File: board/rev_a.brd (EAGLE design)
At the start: 56 x 25 mm, 12 parts, among them IC1 STM32-M-48, IC2 LM2936DT-5.0, IC3 MCP6004, Q1 35A/25V/8.5mΩ, U1 3.3V/150mA

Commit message: [board] Updated PCB and IOC files
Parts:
- removed IC2: LM2936DT-5.0, national-semiconductor:TO252
- removed U1: 3.3V/150mA, SparkFun-IC-Power:SOT23-5
- added C1: 47pF, resistor:C0603
- added D2, D3: BAT54S, diode:SOT23
- added IC4: 25LC040ST, microchip:TSSOP8
- added LDO1: LM2936DT-5.0, national-semiconductor:TO252
- added LDO2: 3.3V/150mA, SparkFun-IC-Power:SOT23-5
- added MCU: STM32-M-48, pel_stm32:LQFP48
- added OP1: MCP6004, linear:TSSOP14
- added Q2: 600mA/40V, SparkFun-DiscreteSemi:SOT23-3
- added R3: 22K, resistor:R0603
- added R4, R5: 1K, resistor:R0603
- added RN1, RN2: 1K, resistor-dil:0603-ARC
- IC1: value STM32-M-48 -> TJA1027; device pel_stm32:LQFP48 -> misc:SO08
- IC3: value MCP6004 -> MCP2551; device linear:TSSOP14 -> SparkFun-IC-Comms:SO08
- moved R2 54.3 mm to (16.0, 21.0), turned to 180 degrees
- moved IC1 34.2 mm to (5.00, 3.00), turned to 270 degrees
- moved C2 14.0 mm to (37.0, 3.75)
- moved C3 13.1 mm to (20.5, 12.5)
- moved IC3 12.0 mm to (20.5, 3.00), turned to 90 degrees
- moved R1 10.3 mm to (12.5, 21.0)
- moved Q1 5.70 mm to (5.62, 21.0)
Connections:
- net N$4 renamed HEATER_CTRL
- new net CAN_CSN: IC3.8, R3.1
- new net CAN_RX: IC3.4, MCU.45
- new net CAN_TX: IC3.1, MCU.46
- new net KLINE: IC1.6, R5.2
- new net KLINE_PULLUP: R4.1
- new net LED_B: RN1.5
- new net LED_G: RN1.7
- new net LED_R: RN1.6
- new net N$1: Q2.3, R5.1
- new net N$10: OP1.7
- new net N$11: OP1.1
- new net N$3: D1.4, RN1.4
- new net N$4: C1.1, LDO2.4
- new net N$5: D1.6, RN1.2
- new net N$6: D1.5, RN1.3
- new net N$7: Q2.1, R4.2
- new net OUT1: D2.3, IC3.7, OP1.8, RN2.7, RN2.8
- new net OUT1_C: J1.3, RN2.1, RN2.2
- new net OUT2: D3.3, IC3.6, OP1.14, RN2.5, RN2.6
- new net OUT2_C: J1.2, RN2.3, RN2.4
- new net SPI2_CLK: IC4.6, MCU.26
- new net SPI2_CS: IC4.1
- new net SPI2_MISO: IC4.2, MCU.27
- new net SPI2_MOSI: IC4.5, MCU.28
- new net USART_CS: IC1.2
- new net USART_RX: IC1.1
- new net USART_TX: IC1.4
- net 12V: now also IC1.7, LDO1.1, Q2.2; no longer IC2.1
- net 5V: now also D1.2, D1.3, D2.2, D3.2, IC3.3, LDO1.3, LDO2.1, LDO2.3, OP1.4; no longer IC2.3, IC3.4, U1.1, U1.3
- net GND: now also C1.2, D2.1, D3.1, IC1.5, IC3.2, IC4.3, IC4.4, IC4.7, LDO1.2, LDO2.2, MCU.23, MCU.35, MCU.47, OP1.11, R3.2; no longer IC1.23, IC1.35, IC1.47, IC2.2, IC3.11, U1.2
- net VBAT: now also MCU.1; no longer IC1.1
- net VCC: now also IC1.3, IC4.8, LDO2.5, MCU.24, MCU.36, MCU.48, MCU.9; no longer IC1.24, IC1.36, IC1.48, IC1.9, U1.5
- net VSSA: now also MCU.8; no longer IC1.8

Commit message: [board] Cleaning up
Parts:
- removed IC1: TJA1027, misc:SO08
- removed IC4: 25LC040ST, microchip:TSSOP8
- removed Q2: 600mA/40V, SparkFun-DiscreteSemi:SOT23-3
- removed R1, R4, R5: 1K, resistor:R0603
- removed R2: 10K, resistor:R0603
- added RN3: 1K, resistor-dil:0603-ARC
- added S1: (no value), SparkFun-Switches:TACTILE_SWITCH_SMD_5.2MM
- moved C1 127.7 mm to (40.5, 22.0), turned to 90 degrees
- moved R3 56.1 mm to (11.0, 1.00)
- moved D1 19.5 mm to (31.0, 3.00)
- moved RN1 19.5 mm to (36.5, 3.25)
- moved C2 19.1 mm to (42.5, 22.0), turned to 90 degrees
- moved LDO2 18.6 mm to (37.6, 21.9), turned to 180 degrees
- moved IC3 16.5 mm to (4.00, 3.00)
- moved OP1 8.25 mm to (27.0, 20.8), turned to 90 degrees
- moved C3 2.50 mm to (20.5, 10.0), turned to 90 degrees
- moved MCU 0.15 mm to (37.6, 12.7), turned to 90 degrees
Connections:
- net CAN_CSN renamed N$8
- removed net KLINE: IC1.6, R5.2
- removed net KLINE_PULLUP: R4.1
- removed net LED_B: RN1.5
- removed net LED_G: RN1.7
- removed net LED_R: RN1.6
- removed net OUT1_C: J1.3, RN2.1, RN2.2
- removed net OUT2_C: J1.2, RN2.3, RN2.4
- removed net SPI2_CLK: IC4.6, MCU.26
- removed net SPI2_CS: IC4.1
- removed net SPI2_MISO: IC4.2, MCU.27
- removed net SPI2_MOSI: IC4.5, MCU.28
- removed net USART_CS: IC1.2
- removed net USART_RX: IC1.1
- removed net USART_TX: IC1.4
- new net AN1: MCU.10
- new net AN2: MCU.16
- new net AN3: MCU.17
- new net BUTTON1: MCU.2, S1.1, S1.2
- new net CAN_RS: MCU.3, R3.2
- new net DAC1: MCU.14
- new net DAC2: MCU.15
- new net NRST: MCU.7
- new net OPA1_IN+: MCU.11
- new net OPA1_IN-: MCU.13
- new net OPA1_OUT: MCU.12
- new net OPA3_IN+: MCU.18
- new net OPA3_IN-: MCU.20
- new net OPA3_OUT: MCU.19
- new net OPA4_IN+: MCU.22
- new net OPA4_IN-: MCU.21
- new net OPA4_OUT: MCU.25
- new net OUT1_PROT: D2.3, MCU.30, OP1.8, RN2.7, RN2.8
- new net OUT2_PROT: D3.3, MCU.31, OP1.14, RN2.5, RN2.6
- new net SWDCLK: MCU.37
- new net SWDIO: MCU.34
- new net TIM2_CH2: MCU.28
- new net TIM4_CH1: MCU.42, RN1.5
- new net TIM4_CH2: MCU.43, RN1.7
- new net TIM4_CH3: MCU.45, RN1.6
- new net TIM4_CH4: MCU.46
- net 12V: no longer IC1.7, Q2.2
- net 5V: now also D1.1
- net CAN_RX: now also MCU.32; no longer MCU.45
- net CAN_TX: now also MCU.33; no longer MCU.46
- net GND: now also RN3.5, S1.3, S1.4; no longer IC1.5, IC4.3, IC4.4, IC4.7, R2.1, R3.2
- net HEATER_CTRL: now also MCU.27, RN3.1, RN3.2; no longer R1.1, R2.2
- net N$1: now also Q1.1, RN3.8; no longer Q2.3, R5.1
- net N$2: now also RN3.3, RN3.7; no longer Q1.1, R1.2
- net N$7: now also RN3.4, RN3.6; no longer Q2.1, R4.2
- net OUT1: now also J1.3, RN2.1, RN2.2; no longer D2.3, OP1.8, RN2.7, RN2.8
- net OUT2: now also J1.2, RN2.3, RN2.4; no longer D3.3, OP1.14, RN2.5, RN2.6
- net VCC: now also MCU.44; no longer IC1.3, IC4.8

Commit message: [board] Testing a few configurations
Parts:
- removed OP1: MCP6004, linear:TSSOP14
- added C4, C5, C6: 100nF, resistor:C0603
- added D4: BAT54S, diode:SOT23
- added J3: (no value), SparkFun-Connectors:1X04_LOCK
- added LDO3: 3.3V/150mA, SparkFun-IC-Power:SOT23-5
- added OPA5: MCP602ST, linear:TSSOP8
- added R1, R4: 20K, resistor:R0603
- added R2, R5: 10K, resistor:R0603
- added R6: 330K, resistor:R0603
- added R7: 22K, resistor:R0603
- added RN4: 1K, resistor-dil:0603-ARC
- D1: value (none) -> BAT54S; device SparkFun-LED:LED-TRICOLOR-5050 -> diode:SOT23
- J1: device SparkFun-Connectors:1X04_LOCK_LONGPADS -> SparkFun-Connectors:1X06_LONGPADS
- LDO1: value LM2936DT-5.0 -> LM2931DT-5.0
- MCU: value STM32-M-48 -> STM32F303CB
- moved Q1 32.8 mm to (38.4, 21.0), turned to 270 degrees
- moved C1 22.9 mm to (18.5, 15.5)
- moved C2 22.2 mm to (23.5, 10.5)
- moved D1 20.7 mm to (10.5, 5.50), turned to 90 degrees
- moved LDO2 20.2 mm to (21.0, 10.5)
- moved S1 20.0 mm to (3.00, 4.00), flipped to the bottom, turned to 90 degrees
- moved RN3 14.5 mm to (29.5, 21.0), turned to 270 degrees
- moved C3 12.3 mm to (25.0, 21.5), turned to 270 degrees
- moved LDO1 9.52 mm to (14.8, 21.2), turned to 270 degrees
- moved R3 8.50 mm to (2.50, 1.00)
- moved D3 8.08 mm to (10.5, 16.0)
- moved D2 8.02 mm to (15.5, 16.0)
- moved RN2 7.00 mm to (6.50, 19.0)
- moved MCU 5.19 mm to (32.8, 11.0), turned to 180 degrees
- moved RN1 2.51 mm to (39.0, 3.00), flipped to the bottom
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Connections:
- removed net N$4: C1.1, LDO2.4
- removed net TIM4_CH1: MCU.42, RN1.5
- removed net TIM4_CH2: MCU.43, RN1.7
- new net N$9: RN1.4, RN1.6
- new net OUT3: IC3.7, J1.3, RN4.1, RN4.2
- new net OUT3_PROT: D1.3, MCU.30, RN4.7, RN4.8
- new net OUT4: IC3.6, J1.2, RN4.3, RN4.4
- new net OUT4_PROT: D4.3, MCU.31, RN4.5, RN4.6
- new net SCL: J3.3, MCU.42, RN1.3
- new net SDA: J3.4, MCU.43, RN1.1
- new net VDDA: C6.1, LDO3.5, MCU.9
- net 12V: now also J1.6; no longer J1.4
- net 5V: now also C5.1, D4.2, J3.2, LDO3.1, LDO3.3, OPA5.8, RN1.5, RN1.7; no longer D1.1, D1.3, OP1.4
- net BUTTON1: now also C4.1
- net DAC1: now also OPA5.3
- net DAC2: now also OPA5.5
- net GND: now also C4.2, C5.2, C6.2, D1.1, D4.1, J3.1, LDO3.2, MCU.44, OPA5.4, R1.1, R4.1; no longer OP1.11
- net IP: now also R7.1
- net N$10: now also R6.1, R7.2; no longer OP1.7
- net N$11: now also C1.1, LDO3.4; no longer OP1.1
- net N$3: now also RN1.2, RN1.8; no longer D1.4, RN1.4
- net N$5: now also OPA5.2, R1.2, R2.2; no longer D1.6, RN1.2
- net N$6: now also R4.2, R5.2; no longer D1.5, RN1.3
- net OPA3_OUT: now also R6.2
- net OUT1: now also J1.5; no longer IC3.7, J1.3
- net OUT1_PROT: now also OPA5.1, R2.1; no longer MCU.30, OP1.8
- net OUT2: now also J1.4; no longer IC3.6, J1.2
- net OUT2_PROT: now also OPA5.7, R5.1; no longer MCU.31, OP1.14
- net TIM4_CH3: no longer RN1.6
- net VCC: no longer MCU.44, MCU.9
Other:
- outline, holes or cut-outs redrawn

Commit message: [board] Working on schema
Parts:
- added C8, C9: 100nF, resistor:C0603
- added D5: BAT54S, diode:SOT23
- added IC1: MCP604ST, linear:TSSOP14
- added R11, R12: 10K, resistor:R0603
- added R8: 20K 1%, resistor:R0603
- added R9: 1K 1%, resistor:R0603
- added X1: B4B-ZR, con-jst:B4B-ZR
- C1: value 47pF -> 100nF
- LDO1: value LM2931DT-5.0 -> LM2931-5.0
- LDO2, LDO3: value 3.3V/150mA -> LDK120DM33R
- Q1: value 35A/25V/8.5mΩ -> Logic level FET
- R1, R4: value 20K -> 20K 1%
- R2, R5: value 10K -> 10K 1%
- moved C4 24.4 mm to (1.50, -22.0), flipped to the top, turned to 0 degrees
- moved C3 2.50 mm to (22.5, 21.5), flipped to the bottom
- moved R6 2.06 mm to (26.0, 2.50)
- moved MCU 2.00 mm to (32.8, 9.00)
- moved R7 1.80 mm to (30.0, 2.00)
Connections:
- net HEATER_CTRL renamed TIM15_CH1
- net TIM2_CH2 renamed TIM15_CH2
- removed net SWDCLK: MCU.37
- new net N$13: C9.1, OPA5.3, R12.2
- new net N$4: C8.1, OPA5.5, R11.2
- new net PUMP_DRV: IC1.1, IC1.2
- new net PUMP_REF: IC1.6, IC1.7
- new net SWCLK: MCU.37, X1.1
- net 12V: now also R8.1
- net 5V: no longer RN1.5, RN1.7
- net AN3: now also D5.3, R8.2, R9.2
- net BUTTON1: no longer C4.1
- net DAC1: now also IC1.3; no longer OPA5.3
- net DAC2: now also IC1.5; no longer OPA5.5
- net GND: now also C8.2, C9.2, D5.1, IC1.11, R9.1, X1.2
- net N$6: now also OPA5.6
- net NRST: now also C4.1, X1.4
- net OPA1_OUT: now also R6.2
- net OPA3_OUT: no longer R6.2
- net SWDIO: now also X1.3
- net TIM4_CH3: now also R12.1
- net TIM4_CH4: now also R11.1
- net VCC: now also RN1.5, RN1.7
- net VDDA: now also D5.2, IC1.4

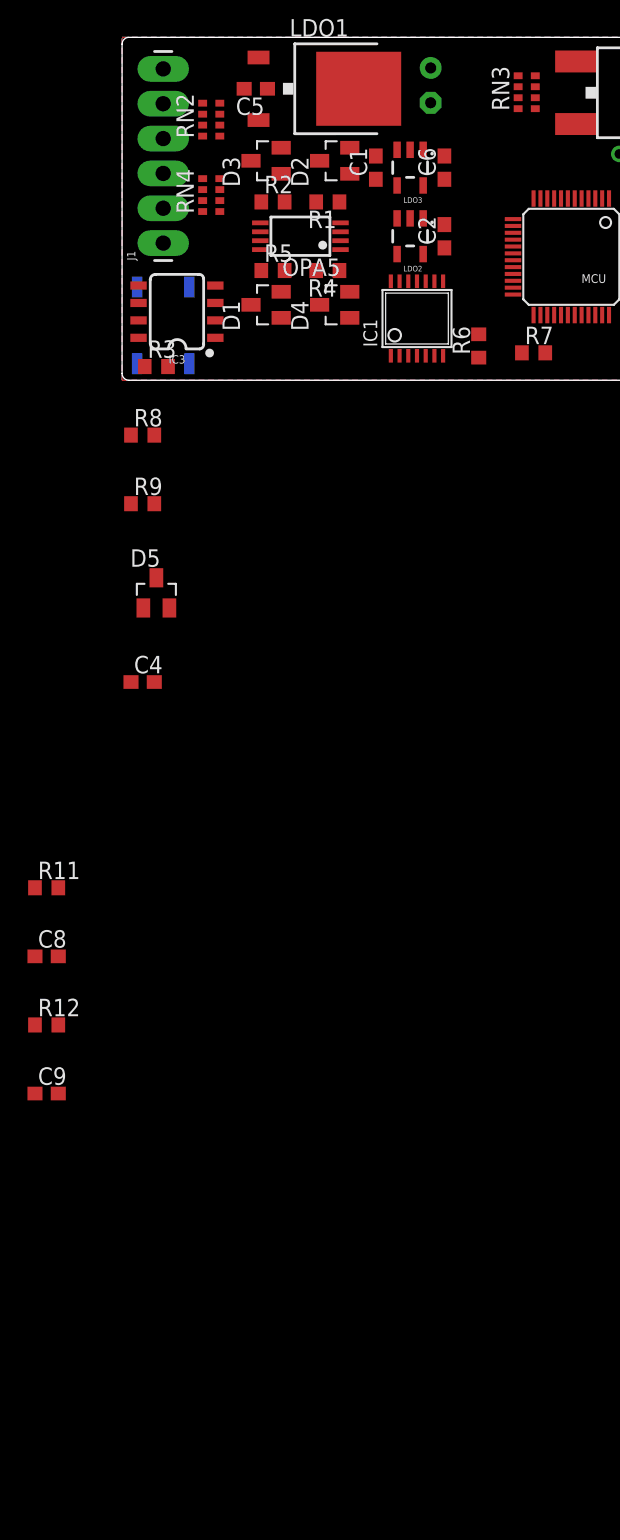
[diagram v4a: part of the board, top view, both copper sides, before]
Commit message: [board] Adding a few analog circuits
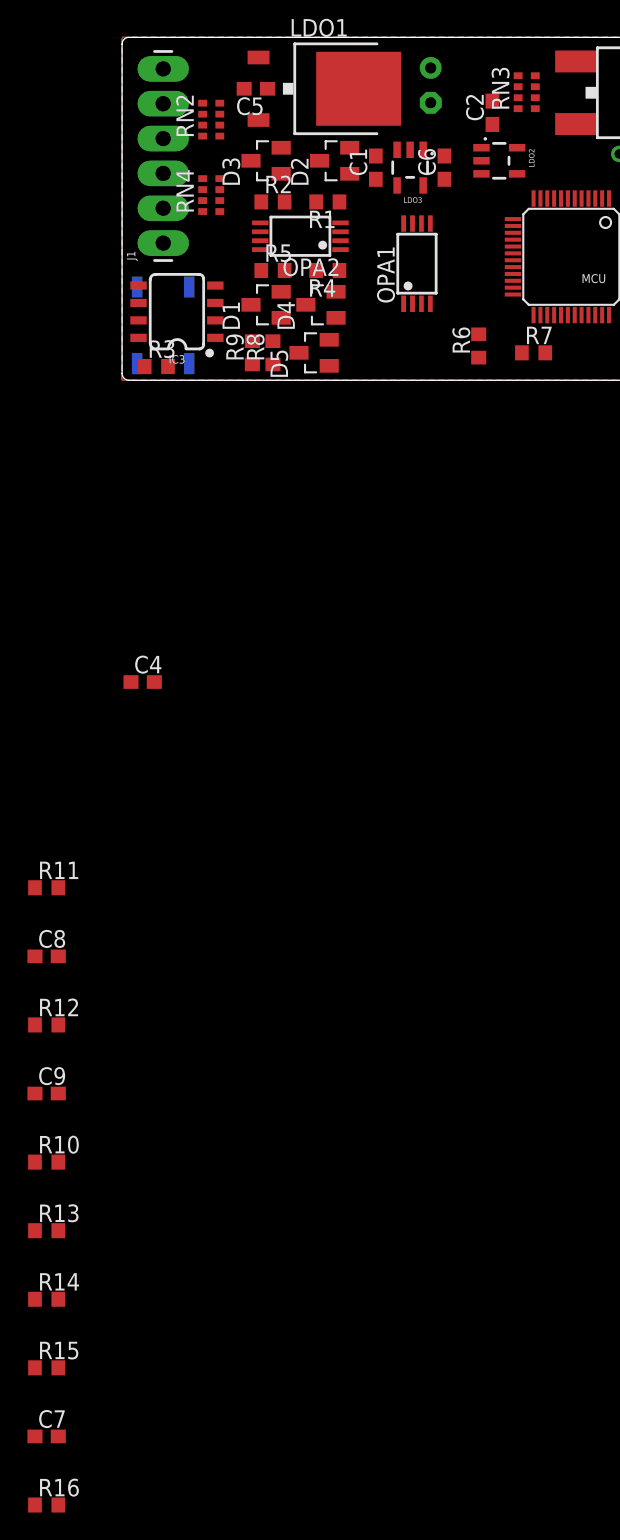
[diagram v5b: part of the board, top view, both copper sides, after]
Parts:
- removed IC1: MCP604ST, linear:TSSOP14
- added C7: 100nF, resistor:C0603
- added OPA1: MCP6002, linear:TSSOP8
- added R10: 22K 1%, resistor:R0603
- added R13: 100K 1%, resistor:R0603
- added R14: 61.9R 1%, resistor:R0603
- added R15: 10K 1%, resistor:R0603
- added R16: 150K 1%, resistor:R0603
- C8, C9: value 100nF -> 10nF
- OPA2: value MCP602ST -> MCP6002
- R11, R12: value 10K -> 10K 1%
- R6: value 330K -> 100K 1%
- R7: value 22K -> 22K 1%
- moved D5 20.9 mm to (14.0, 2.00), turned to 90 degrees
- moved R9 13.6 mm to (9.50, 2.00), turned to 90 degrees
- moved R8 11.2 mm to (11.0, 2.00), turned to 90 degrees
- moved C2 9.66 mm to (27.0, 19.5)
- moved LDO2 8.51 mm to (27.5, 16.0), turned to 270 degrees
- moved D4 1.00 mm to (14.5, 5.50)
- renumbered OPA5 to OPA2
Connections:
- net OPA4_IN+ renamed VS/OPA4_IN+
- removed net CAL_RES: J2.5
- removed net N$10: R6.1, R7.2
- removed net OPA1_IN+: MCU.11
- removed net OPA1_IN-: MCU.13
- removed net OPA1_OUT: MCU.12, R6.2
- removed net PUMP_DRV: IC1.1, IC1.2
- removed net PUMP_REF: IC1.6, IC1.7
- removed net TIM15_CH2: MCU.28
- removed net VS/IP: J2.2
- new net N$12: C7.1, R15.1
- new net RCAL: J2.5, R10.1, R14.2
- new net TIM1_CH1: MCU.29, R15.2
- new net VS/IP_REF: J2.2, OPA1.6, OPA1.7, R13.2
- net AN1: now also D5.3, R8.2, R9.2
- net AN2: now also MCU.11; no longer MCU.16
- net AN3: now also MCU.12; no longer D5.3, MCU.17, R8.2, R9.2
- net DAC1: now also OPA1.3; no longer IC1.3
- net DAC2: now also OPA1.5; no longer IC1.5
- net GND: now also OPA1.4; no longer IC1.11
- net IP: now also OPA1.1, OPA1.2, R14.1
- net N$1: now also RN3.2
- net OPA3_IN+: now also R10.2, R13.1
- net OPA3_IN-: now also R6.1, R7.2
- net OPA3_OUT: now also R6.2
- net TIM15_CH1: no longer RN3.2
- net VDDA: now also OPA1.8; no longer IC1.4
- net VS: now also C7.2

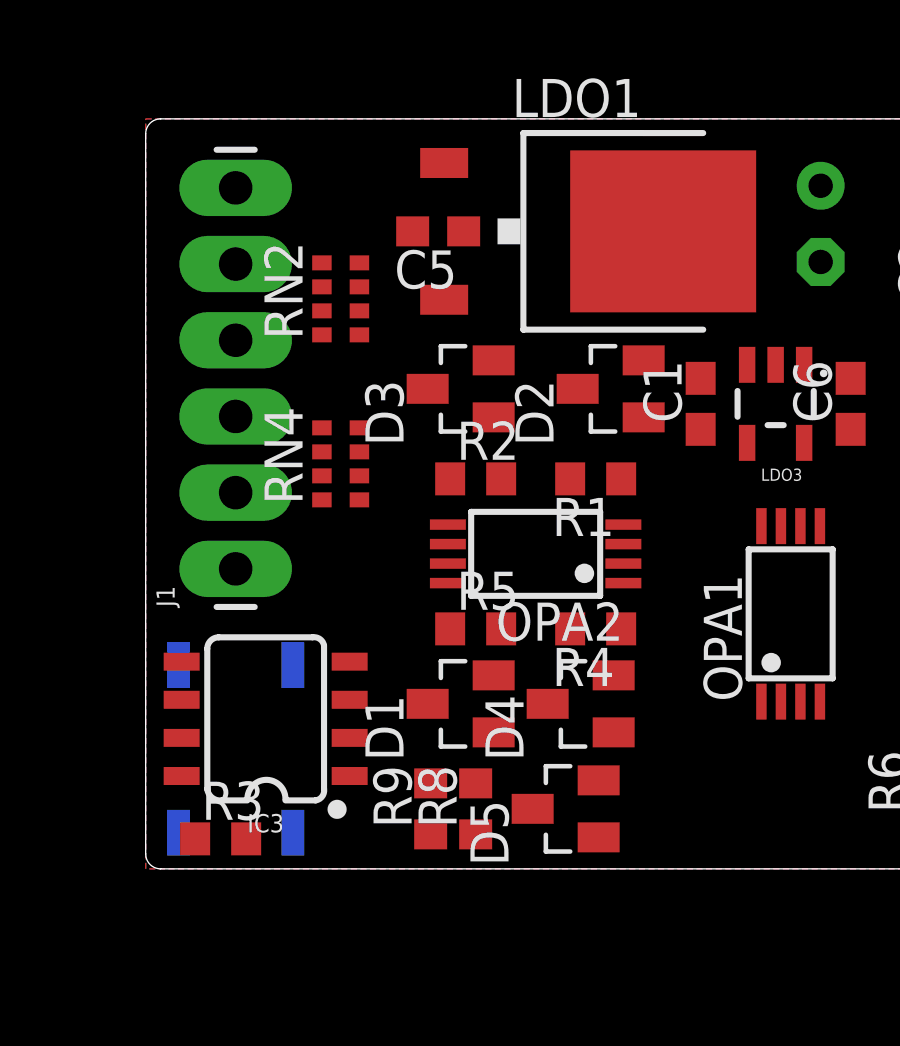
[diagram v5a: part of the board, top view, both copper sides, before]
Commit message: [board] Replacing diodes with smaller packages
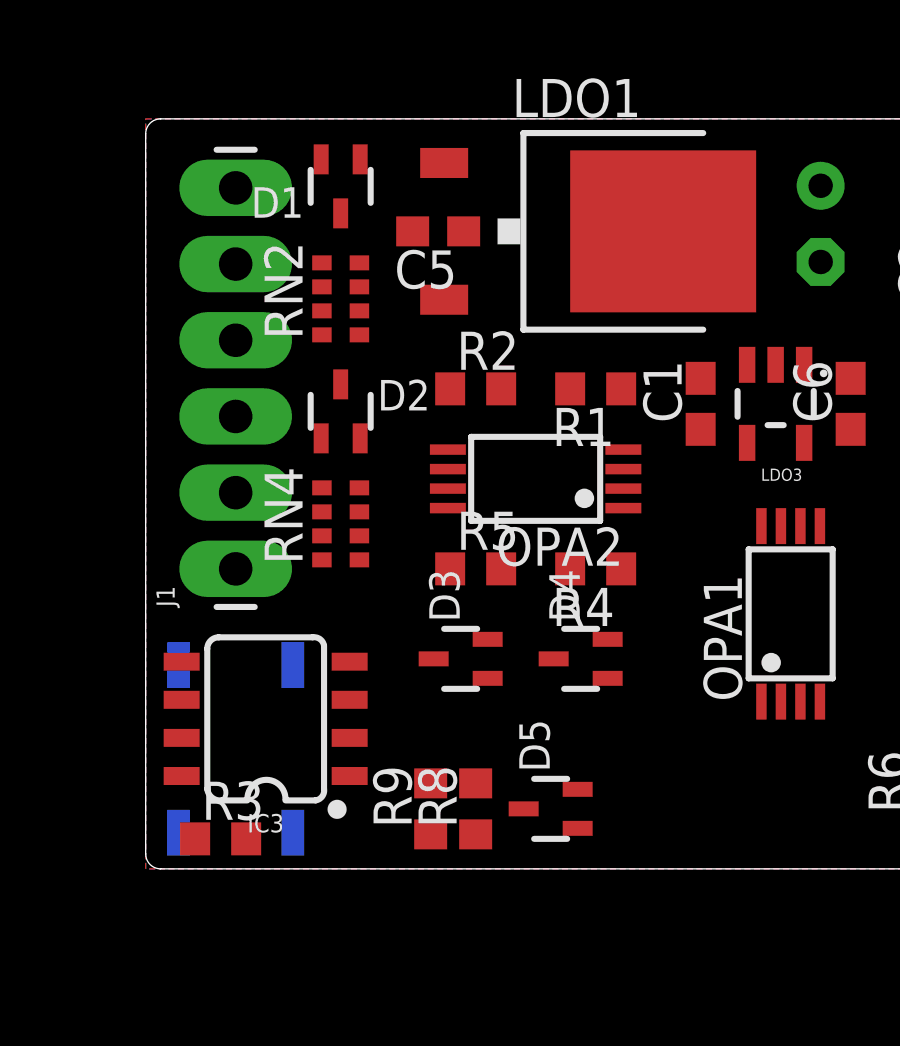
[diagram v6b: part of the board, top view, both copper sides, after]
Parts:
- D1, D2, D3, D4, D5: value BAT54S -> (none); device diode:SOT23 -> zetex:SOT323
- moved D1 17.7 mm to (6.50, 22.8), turned to 180 degrees
- moved D2 9.03 mm to (6.50, 15.2), turned to 0 degrees
- moved D3 9.00 mm to (10.5, 7.00)
- moved R1 3.00 mm to (15.0, 16.0)
- moved R2 3.00 mm to (11.0, 16.0)
- moved OPA2 2.50 mm to (13.0, 13.0)
- moved R4 2.00 mm to (15.0, 10.0)
- moved R5 2.00 mm to (11.0, 10.0)
- moved RN4 2.00 mm to (6.50, 11.5)
- moved D4 1.50 mm to (14.5, 7.00)
- moved D5 0.50 mm to (13.5, 2.00)
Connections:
- net AN1: now also D5.1; no longer D5.3
- net GND: now also D1.3, D2.3, D3.3, D4.3, D5.3; no longer D1.1, D2.1, D3.1, D4.1, D5.1
- net OUT1_PROT: now also D1.1; no longer D2.3
- net OUT2_PROT: now also D2.1; no longer D3.3
- net OUT3_PROT: now also D3.1; no longer D1.3
- net OUT4_PROT: now also D4.1; no longer D4.3
